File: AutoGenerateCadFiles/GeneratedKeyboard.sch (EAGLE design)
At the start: 177 parts

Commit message: Changed Plate files after modifying keyboard layout
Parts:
- removed DF10, DF2, DF4, DF6, DF8: 1N4148, Components:DIODE-DO-35
- removed F10, F2, F4, F6, F8: KEYSWITCH-LED-MX-1U-LED, Keyboard:KEYSWITCH-LED-MX-1U-LED
- removed U$1: ARDUINO-TEENSY++, teensypp:ARDUINO-TEENSY++
- added _1: TEENSY, teensy:TEENSY
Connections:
- removed net PINC0: 6.P0, B.P0, G.P0, SPACE.P0, U$1.10, Y.P0
- removed net PINC1: 5.P0, F.P0, T.P0, U$1.11, V.P0
- removed net PINC2: 4.P0, C.P0, D.P0, R.P0, U$1.12
- removed net PINC3: 3.P0, E.P0, S.P0, U$1.13, X.P0
- removed net PINC4: 2.P0, A.P0, ALT.P0, U$1.14,PWM, W.P0, Z.P0
- removed net PINC5: 1.P0, Q.P0, U$1.15,PWM, WIN.P0
- removed net PNF3: U$1.40,A2
- new net N$1: DKP_DASH.A, KP_DASH.P1
- new net N$10: 5.P1, D5.A
- new net N$11: 6.P1, D6.A
- new net N$12: 7.P1, D7.A
- new net N$13: 8.P1, D8.A
- new net N$14: 9.P1, D9.A
- new net N$15: 0.P1, D0.A
- new net N$16: DASH.P1, DDASH.A
- new net N$17: DEQUAL.A, EQUAL.P1
- new net N$18: BACKSPACE.P1, DBACKSPACE.A
- new net N$19: DF1.A, F1.P1
- new net N$2: DKP_SLASH.A, KP_SLASH.P1
- new net N$20: DF3.A, F3.P1
- new net N$21: BACKSLASH.P1, DBACKSLASH.A
- new net N$22: DRBRACKET.A, RBRACKET.P1
- new net N$23: DLBRACKET.A, LBRACKET.P1
- new net N$24: DP.A, P.P1
- new net N$25: DO.A, O.P1
- new net N$26: DI.A, I.P1
- new net N$27: DU.A, U.P1
- new net N$28: DY.A, Y.P1
- new net N$29: DT.A, T.P1
- new net N$3: DKP_ASTERISK.A, KP_ASTERISK.P1
- new net N$30: DR.A, R.P1
- new net N$31: DE.A, E.P1
- new net N$32: DW.A, W.P1
- new net N$33: DQ.A, Q.P1
- new net N$34: DTAB.A, TAB.P1
- new net N$35: DKP_9.A, KP_9.P1
- new net N$36: DKP_8.A, KP_8.P1
- new net N$37: DKP_7.A, KP_7.P1
- new net N$38: DEQUAL2.A, EQUAL2.P1
- new net N$39: DKP_4.A, KP_4.P1
- new net N$4: DNUMLOCK.A, NUMLOCK.P1
- new net N$40: DKP_5.A, KP_5.P1
- new net N$41: DKP_6.A, KP_6.P1
- new net N$42: CAPSLOCK.P1, DCAPSLOCK.A
- new net N$43: A.P1, DA.A
- new net N$44: DS.A, S.P1
- new net N$45: D.P1, DD.A
- new net N$46: DF.A, F.P1
- new net N$47: DG.A, G.P1
- new net N$48: DH.A, H.P1
- new net N$49: DJ.A, J.P1
- new net N$5: DESC.A, ESC.P1
- new net N$50: DK.A, K.P1
- new net N$51: DL.A, L.P1
- new net N$52: DSEMICOLON.A, SEMICOLON.P1
- new net N$53: DQUOTE.A, QUOTE.P1
- new net N$54: DENTER.A, ENTER.P1
- new net N$55: DF5.A, F5.P1
- new net N$56: DF7.A, F7.P1
- new net N$57: DSHIFT2.A, SHIFT2.P1
- new net N$58: DSLASH.A, SLASH.P1
- new net N$59: DPERIOD.A, PERIOD.P1
- new net N$6: 2.P1, D2.A
- new net N$60: COMMA.P1, DCOMMA.A
- new net N$61: DM.A, M.P1
- new net N$62: DN.A, N.P1
- new net N$63: B.P1, DB.A
- new net N$64: DV.A, V.P1
- new net N$65: C.P1, DC.A
- new net N$66: DX.A, X.P1
- new net N$67: DZ.A, Z.P1
- new net N$68: DSHIFT.A, SHIFT.P1
- new net N$69: DKP_3.A, KP_3.P1
- new net N$7: 3.P1, D3.A
- new net N$70: DKP_2.A, KP_2.P1
- new net N$71: DKP_1.A, KP_1.P1
- new net N$72: DENTER2.A, ENTER2.P1
- new net N$73: DKP_DEL.A, KP_DEL.P1
- new net N$74: DKP_0.A, KP_0.P1
- new net N$75: CTRL.P1, DCTRL.A
- new net N$76: DWIN.A, WIN.P1
- new net N$77: ALT.P1, DALT.A
- new net N$78: DSPACE.A, SPACE.P1
- new net N$79: ALT2.P1, DALT2.A
- new net N$8: 1.P1, D1.A
- new net N$80: DWIN2.A, WIN2.P1
- new net N$81: DMENU.A, MENU.P1
- new net N$82: CTRL2.P1, DCTRL2.A
- new net N$83: DF9.A, F9.P1
- new net N$9: 4.P1, D4.A
- new net PINB0: _1._B0
- new net PINE6: EQUAL.P0, MENU.P0, QUOTE.P0, RBRACKET.P0, _1._E6
- new net PINF3: 8.P0, I.P0, J.P0, M.P0
- new net PINF7: 5.P0, F.P0, T.P0, V.P0, _1._F7
- net PINB1: now also _1._B1; no longer DF2.C, U$1.21
- net PINB2: now also _1._B2; no longer DF4.C, U$1.22
- net PINB3: now also _1._B3; no longer DF6.C, U$1.23
- net PINB4: now also _1._B4; no longer DF8.C, U$1.24,PWM
- net PINB5: now also _1._B5; no longer DF10.C, U$1.25,PWM
- net PINB6: now also F1.P0, F3.P0, F5.P0, F7.P0, F9.P0, _1._B6; no longer F10.P0, F2.P0, F4.P0, F6.P0, F8.P0, U$1.26,PWM
- net PINB7: now also BACKSLASH.P0, BACKSPACE.P0, CTRL2.P0, ENTER.P0, SHIFT2.P0, _1._B7; no longer F1.P0, F3.P0, F5.P0, F7.P0, F9.P0, U$1.27,PWM
- net PINC6: now also ENTER2.P0, EQUAL2.P0, KP_DASH.P0, _1._C6; no longer CAPSLOCK.P0, CTRL.P0, ESC.P0, SHIFT.P0, TAB.P0, U$1.16,PWM
- net PINC7: now also _1._C7; no longer KP_0.P0, KP_3.P0, KP_6.P0, KP_9.P0, NUMLOCK.P0, U$1.17
- net PIND0: now also 4.P0, C.P0, D.P0, R.P0, _1._D0; no longer BACKSLASH.P0, BACKSPACE.P0, CTRL2.P0, ENTER.P0, SHIFT2.P0, U$1.0,PWM,INT0
- net PIND1: now also 3.P0, E.P0, S.P0, X.P0, _1._D1; no longer EQUAL.P0, MENU.P0, QUOTE.P0, RBRACKET.P0, U$1.1,PWM,INT1
- net PIND2: now also 2.P0, A.P0, ALT.P0, W.P0, Z.P0, _1._D2; no longer DASH.P0, LBRACKET.P0, SEMICOLON.P0, SLASH.P0, U$1.2,RX,INT2, WIN2.P0
- net PIND3: now also 1.P0, CAPSLOCK.P0, CTRL.P0, ESC.P0, Q.P0, SHIFT.P0, TAB.P0, WIN.P0, _1._D3; no longer 0.P0, ALT2.P0, L.P0, P.P0, PERIOD.P0, U$1.3,TX,INT3
- net PIND4: now also KP_0.P0, KP_3.P0, KP_6.P0, KP_9.P0, NUMLOCK.P0, _1._D4; no longer 9.P0, COMMA.P0, K.P0, O.P0, U$1.4
- net PIND5: now also KP_2.P0, KP_5.P0, KP_8.P0, KP_ASTERISK.P0, _1._D5; no longer 8.P0, I.P0, J.P0, M.P0, U$1.5
- net PIND7: now also KP_1.P0, KP_4.P0, KP_7.P0, KP_DEL.P0, KP_SLASH.P0, _1._D7; no longer 7.P0, H.P0, N.P0, U$1.7, U.P0
- net PINF0: now also DASH.P0, LBRACKET.P0, SEMICOLON.P0, SLASH.P0, WIN2.P0, _1._F0; no longer KP_2.P0, KP_5.P0, KP_8.P0, KP_ASTERISK.P0, U$1.38,A0
- net PINF1: now also 0.P0, ALT2.P0, L.P0, P.P0, PERIOD.P0, _1._F1; no longer KP_1.P0, KP_4.P0, KP_7.P0, KP_DEL.P0, KP_SLASH.P0, U$1.39,A1
- net PINF2: now also 9.P0, COMMA.P0, K.P0, O.P0; no longer ENTER2.P0, EQUAL2.P0, KP_DASH.P0
- net PINF4: now also 7.P0, H.P0, N.P0, U.P0, _1._F4; no longer U$1.41,A3
- net PINF5: now also _1._F5; no longer U$1.42,A4
- net PINF6: now also 6.P0, B.P0, G.P0, SPACE.P0, Y.P0, _1._F6; no longer U$1.43,A5

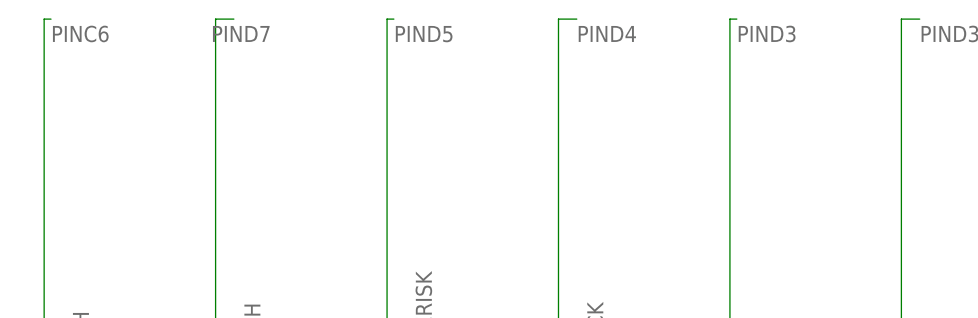
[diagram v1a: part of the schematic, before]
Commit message: Fixed an issue where 2 columns were connected together
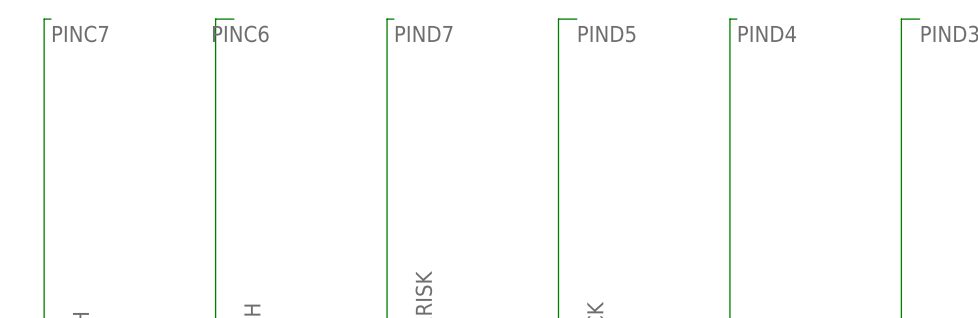
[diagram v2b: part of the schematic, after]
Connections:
- net PINC6: now also KP_1.P0, KP_4.P0, KP_7.P0, KP_DEL.P0, KP_SLASH.P0; no longer ENTER2.P0, EQUAL2.P0, KP_DASH.P0
- net PINC7: now also ENTER2.P0, EQUAL2.P0, KP_DASH.P0
- net PIND3: no longer CAPSLOCK.P0, CTRL.P0, ESC.P0, SHIFT.P0, TAB.P0
- net PIND4: now also CAPSLOCK.P0, CTRL.P0, ESC.P0, SHIFT.P0, TAB.P0; no longer KP_0.P0, KP_3.P0, KP_6.P0, KP_9.P0, NUMLOCK.P0
- net PIND5: now also KP_0.P0, KP_3.P0, KP_6.P0, KP_9.P0, NUMLOCK.P0; no longer KP_2.P0, KP_5.P0, KP_8.P0, KP_ASTERISK.P0
- net PIND7: now also KP_2.P0, KP_5.P0, KP_8.P0, KP_ASTERISK.P0; no longer KP_1.P0, KP_4.P0, KP_7.P0, KP_DEL.P0, KP_SLASH.P0
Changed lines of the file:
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@@
 <label x="96.52" y="33.02" size="1.778" layer="95"/>
+</segment>
+</net>
+<net name="PIND4" class="0">
+<segment>
+<pinref part="_1" gate="G$1" pin="_D4"/>
+<wire x1="515.62" y1="-30.48" x2="500.38" y2="-30.48" width="0.1524" layer="91"/>
+<label x="502.92" y="-30.48" size="1.778" layer="95"/>
 </segment>
 <segment>
@@
 </segment>
 </net>
-<net name="PIND4" class="0">
+<net name="PIND5" class="0">
 <segment>
-<pinref part="_1" gate="G$1" pin="_D4"/>
-<wire x1="515.62" y1="-30.48" x2="500.38" y2="-30.48" width="0.1524" layer="91"/>
-<label x="502.92" y="-30.48" size="1.778" layer="95"/>
+<pinref part="_1" gate="G$1" pin="_D5"/>
+<wire x1="515.62" y1="-33.02" x2="500.38" y2="-33.02" width="0.1524" layer="91"/>
+<label x="502.92" y="-33.02" size="1.778" layer="95"/>
 </segment>
 <segment>
@@
 </segment>
 </net>
-<net name="PIND5" class="0">
+<net name="PIND7" class="0">
 <segment>
-<pinref part="_1" gate="G$1" pin="_D5"/>
-<wire x1="515.62" y1="-33.02" x2="500.38" y2="-33.02" width="0.1524" layer="91"/>
-<label x="502.92" y="-33.02" size="1.778" layer="95"/>
+<pinref part="_1" gate="G$1" pin="_D7"/>
+<wire x1="515.62" y1="-38.1" x2="500.38" y2="-38.1" width="0.1524" layer="91"/>
+<label x="502.92" y="-38.1" size="1.778" layer="95"/>
 </segment>
 <segment>
@@
 </segment>
 </net>
-<net name="PIND7" class="0">
+<net name="PINC6" class="0">
 <segment>
-<pinref part="_1" gate="G$1" pin="_D7"/>
-<wire x1="515.62" y1="-38.1" x2="500.38" y2="-38.1" width="0.1524" layer="91"/>
-<label x="502.92" y="-38.1" size="1.778" layer="95"/>
+<pinref part="_1" gate="G$1" pin="_C6"/>
+<wire x1="515.62" y1="-60.96" x2="500.38" y2="-60.96" width="0.1524" layer="91"/>
+<label x="502.92" y="-60.96" size="1.778" layer="95"/>
 </segment>
 <segment>
@@
 </segment>
 </net>
-<net name="PINC6" class="0">
+<net name="PINC7" class="0">
 <segment>
-<pinref part="_1" gate="G$1" pin="_C6"/>
-<wire x1="515.62" y1="-60.96" x2="500.38" y2="-60.96" width="0.1524" layer="91"/>
-<label x="502.92" y="-60.96" size="1.778" layer="95"/>
+<pinref part="_1" gate="G$1" pin="_C7"/>
+<wire x1="515.62" y1="-63.5" x2="500.38" y2="-63.5" width="0.1524" layer="91"/>
+<label x="502.92" y="-63.5" size="1.778" layer="95"/>
 </segment>
 <segment>
@@
 </segment>
 </net>
-<net name="PINC7" class="0">
-<segment>
-<pinref part="_1" gate="G$1" pin="_C7"/>
-<wire x1="515.62" y1="-63.5" x2="500.38" y2="-63.5" width="0.1524" layer="91"/>
-<label x="502.92" y="-63.5" size="1.778" layer="95"/>
-</segment>
-</net>
